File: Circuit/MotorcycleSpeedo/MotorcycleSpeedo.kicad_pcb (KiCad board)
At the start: 2 copper layers, 2 parts

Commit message: Board built enough to submit. I'm sure changes will be made.
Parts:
- removed REF** (x2): x25FrontStepper, X25Stepper:x25FrontStepper
- added BT101: Battery_Cell, Battery:BatteryHolder_Keystone_1060_1x2032, B.Cu at (240.7, 154.4)
- added C101: C, Capacitor_SMD:C_0603_1608Metric, B.Cu at (244.7, 167.8)
- added C102: C, Capacitor_SMD:C_0603_1608Metric, B.Cu at (246.3, 167.8)
- added C103: C, Capacitor_SMD:C_0603_1608Metric, B.Cu at (262.4, 147.8)
- added C104: C, Capacitor_SMD:C_0603_1608Metric, B.Cu at (261.4, 153.6)
- added C105: .1uF, Capacitor_SMD:C_0603_1608Metric, B.Cu at (203.4, 157.6)
- added C106: C, Capacitor_SMD:C_0603_1608Metric, B.Cu at (258.2, 142.6)
- added C107: C, Capacitor_SMD:C_0603_1608Metric, B.Cu at (258.4, 138.5)
- added C108: C, Capacitor_SMD:C_0603_1608Metric, B.Cu at (181.7, 162.2)
- added C109: .1uf, Capacitor_SMD:C_0603_1608Metric, B.Cu at (181.7, 163.8)
- added C110: C, Capacitor_SMD:C_0603_1608Metric, B.Cu at (191.7, 163.4)
- added C111: .1uf, Capacitor_SMD:C_0603_1608Metric, B.Cu at (187.7, 157.0)
- added C112: .1uf, Capacitor_SMD:C_0603_1608Metric, B.Cu at (184.7, 162.7)
- added C113: C, Capacitor_SMD:C_0603_1608Metric, B.Cu at (226.7, 162.2)
- added C114: 100uF, Capacitor_SMD:C_0603_1608Metric, B.Cu at (258.8, 154.2)
- added C115: 1500pf, Capacitor_SMD:C_0603_1608Metric, B.Cu at (259.5, 161.1)
- added C116: CP, Capacitor_SMD:C_0603_1608Metric, B.Cu at (264.4, 166.9)
- added C117: C, Capacitor_SMD:C_0603_1608Metric, B.Cu at (164.7, 173.6)
- added C118: C, Capacitor_SMD:C_0603_1608Metric, B.Cu at (172.8, 173.6)
- added C119: C, Capacitor_SMD:C_0603_1608Metric, B.Cu at (174.3, 169.0)
- added C120: C, Capacitor_SMD:C_0603_1608Metric, B.Cu at (214.8, 162.4)
- added C121: C, Capacitor_SMD:C_0603_1608Metric, B.Cu at (163.3, 156.1)
- added C122: C, Capacitor_SMD:C_0603_1608Metric, B.Cu at (173.1, 152.6)
- added C123: C, Capacitor_SMD:C_0603_1608Metric, B.Cu at (170.0, 142.8)
- added C124: C, Capacitor_SMD:C_0603_1608Metric, B.Cu at (170.0, 141.2)
- added C125: C, Capacitor_SMD:C_0603_1608Metric, B.Cu at (159.2, 143.7)
- added C126: C, Capacitor_SMD:C_0603_1608Metric, B.Cu at (159.2, 145.2)
- added C127: C, Capacitor_SMD:C_0603_1608Metric, B.Cu at (156.9, 144.4)
- added C128: 20pF, Capacitor_SMD:C_0603_1608Metric, B.Cu at (155.4, 151.4)
- added C129: 20pF, Capacitor_SMD:C_0603_1608Metric, B.Cu at (155.4, 148.3)
- added C130: 9pF, Capacitor_SMD:C_0603_1608Metric, B.Cu at (160.6, 157.9)
- added C131: 9pF, Capacitor_SMD:C_0603_1608Metric, B.Cu at (157.5, 158.0)
- added C132: C, Capacitor_SMD:C_0603_1608Metric, B.Cu at (171.6, 124.0)
- added C133: C, Capacitor_SMD:C_0603_1608Metric, B.Cu at (244.2, 125.1)
- added C134: .1uF, Capacitor_SMD:C_0603_1608Metric, B.Cu at (179.9, 117.9)
- added C135: 0.1uF, Capacitor_SMD:C_0603_1608Metric, B.Cu at (180.2, 171.4)
- added C136: 0.22uF, Capacitor_SMD:C_0603_1608Metric, B.Cu at (159.3, 140.7)
- added C137: .1uF, Capacitor_SMD:C_0603_1608Metric, B.Cu at (253.1, 117.7)
- added C138: .1uF, Capacitor_SMD:C_0603_1608Metric, B.Cu at (176.8, 117.9)
- added C139: .1uF, Capacitor_SMD:C_0603_1608Metric, B.Cu at (247.9, 117.6)
- added C140: 0.1uF, Capacitor_SMD:C_0603_1608Metric, B.Cu at (176.6, 171.5)
- added C141: 0.22uF, Capacitor_SMD:C_0603_1608Metric, B.Cu at (160.9, 140.7)
- added C142: .01uF, Capacitor_SMD:C_0603_1608Metric, B.Cu at (202.1, 162.7)
- added C143: .1uF, Capacitor_SMD:C_0603_1608Metric, B.Cu at (213.8, 149.0)
- added C144: .1uF, Capacitor_SMD:C_0603_1608Metric, B.Cu at (213.9, 147.3)
- added C145: C, Capacitor_SMD:C_0603_1608Metric, B.Cu at (157.8, 140.7)
- added C201: 1uF, Capacitor_SMD:C_0603_1608Metric, B.Cu at (261.1, 137.8)
- added C202: 22uF, Capacitor_THT:C_Radial_D5.0mm_H11.0mm_P2.00mm, B.Cu at (257.3, 147.2)
- added C203: DNP, Capacitor_SMD:C_0805_2012Metric, B.Cu at (269.8, 140.5)
- added C204: 22uF, Capacitor_SMD:C_0805_2012Metric, B.Cu at (268.2, 144.8)
- added D101: D_Schottky, Diode_SMD:D_SMA, B.Cu at (241.9, 169.8)
- added D102: D_Schottky, Diode_SMD:D_SMA, B.Cu at (233.2, 169.9)
- added D103: D_TVS, Diode_SMD:D_SMA, B.Cu at (233.2, 166.2)
- added D104: SP721, Package_SO:SOIC-8_3.9x4.9mm_P1.27mm, B.Cu at (158.9, 162.6)
- added D105: LED, LED_SMD:LED_0603_1608Metric_Pad1.05x0.95mm_HandSolder, B.Cu at (270.9, 130.8)
- added D106: LED, LED_SMD:LED_0603_1608Metric_Pad1.05x0.95mm_HandSolder, B.Cu at (273.5, 120.3)
- added D107: LED, LED_SMD:LED_0603_1608Metric_Pad1.05x0.95mm_HandSolder, B.Cu at (273.8, 109.4)
- added D108: LED, LED_SMD:LED_0603_1608Metric_Pad1.05x0.95mm_HandSolder, B.Cu at (271.8, 98.8)
- added D109: LED, LED_SMD:LED_0603_1608Metric_Pad1.05x0.95mm_HandSolder, B.Cu at (267.6, 88.8)
- added D110: LED, LED_SMD:LED_0603_1608Metric_Pad1.05x0.95mm_HandSolder, B.Cu at (261.4, 79.9)
- added D111: LED, LED_SMD:LED_0603_1608Metric_Pad1.05x0.95mm_HandSolder, B.Cu at (253.5, 72.6)
- added D112: LED, LED_SMD:LED_0603_1608Metric_Pad1.05x0.95mm_HandSolder, B.Cu at (244.1, 67.1)
- added D113: LED, LED_SMD:LED_0603_1608Metric_Pad1.05x0.95mm_HandSolder, B.Cu at (233.9, 63.7)
- added D114: LED, LED_SMD:LED_0603_1608Metric_Pad1.05x0.95mm_HandSolder, B.Cu at (223.1, 62.5)
- added D115: LED, LED_SMD:LED_0603_1608Metric_Pad1.05x0.95mm_HandSolder, F.Cu at (225.6, 115.1)
- added D116: LED, LED_SMD:LED_0603_1608Metric_Pad1.05x0.95mm_HandSolder, F.Cu at (225.6, 111.6)
- added D117: LED, LED_SMD:LED_0603_1608Metric_Pad1.05x0.95mm_HandSolder, B.Cu at (156.1, 130.8)
- added D118: LED, LED_SMD:LED_0603_1608Metric_Pad1.05x0.95mm_HandSolder, B.Cu at (153.5, 120.3)
- added D119: D, Diode_SMD:D_SMA, B.Cu at (227.8, 166.7)
- added D120: LED, LED_SMD:LED_0603_1608Metric_Pad1.05x0.95mm_HandSolder, B.Cu at (153.2, 109.4)
- added D121: LED, LED_SMD:LED_0603_1608Metric_Pad1.05x0.95mm_HandSolder, B.Cu at (155.2, 98.8)
- added D122: D, Diode_SMD:D_SMA, B.Cu at (270.1, 162.4)
- added D123: LED, LED_SMD:LED_0603_1608Metric_Pad1.05x0.95mm_HandSolder, B.Cu at (159.4, 88.8)
- added D124: LED, LED_SMD:LED_0603_1608Metric_Pad1.05x0.95mm_HandSolder, B.Cu at (165.6, 80.0)
- added D125: LED, LED_SMD:LED_0603_1608Metric_Pad1.05x0.95mm_HandSolder, B.Cu at (173.5, 72.6)
- added D126: LED, LED_SMD:LED_0603_1608Metric_Pad1.05x0.95mm_HandSolder, B.Cu at (182.8, 67.1)
- added D127: LED, LED_SMD:LED_0603_1608Metric_Pad1.05x0.95mm_HandSolder, B.Cu at (193.1, 63.7)
- added D128: LED, LED_SMD:LED_0603_1608Metric_Pad1.05x0.95mm_HandSolder, B.Cu at (203.8, 62.6)
- added D129: LED, LED_SMD:LED_0603_1608Metric_Pad1.05x0.95mm_HandSolder, F.Cu at (201.9, 115.0)
- added D130: LED, LED_SMD:LED_0603_1608Metric_Pad1.05x0.95mm_HandSolder, F.Cu at (202.4, 111.3)
- added D131: D, Diode_SMD:D_SMA, B.Cu at (216.4, 166.9)
- added D132: HIGH, Indicators:HF.SilkSF.Cu, F.Cu at (206.9, 82.0)
- added D133: RIGHT, Indicators:RightPointingF.SilkSF.Cu, F.Cu at (232.4, 82.0)
- added D134: LEFT, Indicators:LeftPointingF.SilkSF.Cu, F.Cu at (194.4, 82.5)
- added D135: NEUTRAL, Indicators:NF.SilkSF.Cu, F.Cu at (220.4, 82.0)
- added F101: Polyfuse, Fuse:Fuse_1206_3216Metric, B.Cu at (238.1, 169.9)
- added H101: MountingHole_Pad, MountingHole:MountingHole_3.2mm_M3_DIN965_Pad, F.Cu at (243.8, 96.4)
- added H102: MountingHole_Pad, MountingHole:MountingHole_3.2mm_M3_DIN965_Pad, F.Cu at (213.8, 125.0)
- added H103: MountingHole_Pad, MountingHole:MountingHole_3.2mm_M3_DIN965_Pad, F.Cu at (213.8, 60.4)
- added H104: MountingHole_Pad, MountingHole:MountingHole_3.2mm_M3_DIN965_Pad, F.Cu at (273.9, 171.6)
- added H105: MountingHole_Pad, MountingHole:MountingHole_3.2mm_M3_DIN965_Pad, F.Cu at (180.9, 96.5)
- added H106: MountingHole_Pad, MountingHole:MountingHole_3.2mm_M3_DIN965_Pad, F.Cu at (157.2, 171.2)
- added J101: Conn_01x07_Female, Connector_PinHeader_2.54mm:PinHeader_1x07_P2.54mm_Vertical, F.Cu at (187.5, 167.4)
- added J102: Conn_01x03_Female, Connector_PinHeader_2.54mm:PinHeader_1x03_P2.54mm_Vertical, B.Cu at (227.1, 172.4)
- added J103: Conn_01x02_Female, Connector_PinHeader_2.54mm:PinHeader_1x02_P2.54mm_Vertical, B.Cu at (167.5, 174.7)
- added J104: Conn_01x03_Female, Connector_PinHeader_2.54mm:PinHeader_1x03_P2.54mm_Vertical, B.Cu at (215.2, 172.5)
- added J105: Conn_01x04_Female, Connector_PinHeader_2.54mm:PinHeader_1x04_P2.54mm_Vertical, B.Cu at (218.1, 73.0)
- added J106: Conn_02x04_Counter_Clockwise, Connector_PinHeader_2.54mm:PinHeader_2x04_P2.54mm_Vertical, B.Cu at (185.3, 148.4)
- added J107: Conn_01x03_Female, Connector_PinHeader_2.54mm:PinHeader_1x03_P2.54mm_Vertical, F.Cu at (238.0, 173.7)
- added J108: Conn_01x04_Male, Connector_PinHeader_1.27mm:PinHeader_1x04_P1.27mm_Vertical, F.Cu at (174.1, 159.7)
- added J109: Conn_01x04_Female, Connector_PinHeader_2.54mm:PinHeader_1x04_P2.54mm_Vertical, F.Cu at (175.8, 174.1)
- added J110: Conn_01x01_Female, TestPoint:TestPoint_Pad_1.5x1.5mm, B.Cu at (163.8, 160.3)
- added JP101: SolderJumper_3_Bridged12, Jumper:SolderJumper-3_P1.3mm_Bridged12_Pad1.0x1.5mm_NumberLabels, B.Cu at (177.8, 162.9)
- added JP102: SolderJumper_3_Bridged12, Jumper:SolderJumper-3_P1.3mm_Bridged12_Pad1.0x1.5mm_NumberLabels, B.Cu at (187.9, 164.6)
- added JP103: SolderJumper_3_Bridged12, Jumper:SolderJumper-3_P1.3mm_Bridged12_Pad1.0x1.5mm_NumberLabels, B.Cu at (207.6, 172.3)
- added JP104: SolderJumper_3_Bridged12, Jumper:SolderJumper-3_P1.3mm_Bridged12_RoundedPad1.0x1.5mm_NumberLabels, B.Cu at (203.4, 91.0)
- added JP105: SolderJumper_3_Bridged12, Jumper:SolderJumper-3_P1.3mm_Bridged12_RoundedPad1.0x1.5mm_NumberLabels, B.Cu at (229.4, 90.5)
- added JP106: SolderJumper_3_Bridged12, Jumper:SolderJumper-3_P1.3mm_Bridged12_RoundedPad1.0x1.5mm_NumberLabels, B.Cu at (198.4, 91.0)
- added JP107: SolderJumper_3_Bridged12, Jumper:SolderJumper-3_P1.3mm_Bridged12_RoundedPad1.0x1.5mm_NumberLabels, B.Cu at (224.4, 90.5)
- added L101: 220, MotorcycleSpeedo:SMSD0804-Inductor, B.Cu at (271.7, 153.3)
- added L201: 10uH, CDRH6D28:CDRH6D28, B.Cu at (263.1, 140.4)
- added M101: Stepper_Motor_bipolar, X25Stepper:x25FrontStepper, F.Cu at (203.8, 113.4)
- added M102: Stepper_Motor_bipolar, X25Stepper:x25FrontStepper, B.Cu at (223.8, 113.4)
- added Q101: Q_NMOS_GSD, Package_TO_SOT_SMD:SOT-23, B.Cu at (252.7, 109.4)
- added Q102: Q_NMOS_GSD, Package_TO_SOT_SMD:SOT-23, B.Cu at (164.1, 119.0)
- added Q103: Q_PMOS_GSD, Package_TO_SOT_SMD:SOT-23, B.Cu at (193.1, 90.3)
- added Q104: Q_NMOS_GSD, Package_TO_SOT_SMD:SOT-23, B.Cu at (193.1, 94.3)
- added R101: R, Resistor_SMD:R_0603_1608Metric, B.Cu at (238.4, 166.8)
- added R102: R, Resistor_SMD:R_0603_1608Metric, B.Cu at (261.6, 125.2)
- added R103: R, Resistor_SMD:R_0603_1608Metric, B.Cu at (261.8, 109.1)
- added R104: R, Resistor_SMD:R_0603_1608Metric, B.Cu at (254.0, 91.8)
- added R105: R, Resistor_SMD:R_0603_1608Metric, B.Cu at (240.2, 80.2)
- added R106: R, Resistor_SMD:R_0603_1608Metric, B.Cu at (240.2, 78.5)
- added R107: 10K, Resistor_SMD:R_0603_1608Metric, B.Cu at (244.9, 137.7)
- added R108: R, Resistor_SMD:R_0603_1608Metric, B.Cu at (219.4, 127.5)
- added R109: 470, Resistor_SMD:R_0603_1608Metric, B.Cu at (244.9, 139.3)
- added R110: 10K, Resistor_SMD:R_0603_1608Metric, B.Cu at (252.5, 112.0)
- added R111: .22, Resistor_SMD:R_0603_1608Metric, B.Cu at (264.5, 153.6)
- added R112: 10K, Resistor_SMD:R_0603_1608Metric, B.Cu at (226.7, 160.6)
- added R113: R, Resistor_SMD:R_0603_1608Metric, B.Cu at (224.9, 168.7)
- added R114: R, Resistor_SMD:R_0603_1608Metric, B.Cu at (165.9, 128.0)
- added R115: 180, Resistor_SMD:R_0603_1608Metric, B.Cu at (265.1, 151.9)
- added R116: R, Resistor_SMD:R_0603_1608Metric, B.Cu at (163.1, 109.4)
- added R117: R, Resistor_SMD:R_0603_1608Metric, B.Cu at (168.0, 93.3)
- added R118: R, Resistor_SMD:R_0603_1608Metric, B.Cu at (262.0, 166.2)
- added R119: R, Resistor_SMD:R_0603_1608Metric, B.Cu at (178.6, 80.1)
- added R120: 120, Resistor_SMD:R_0603_1608Metric, B.Cu at (164.4, 168.9)
- added R121: R, Resistor_SMD:R_0603_1608Metric, B.Cu at (262.0, 167.8)
- added R122: R, Resistor_SMD:R_0603_1608Metric, B.Cu at (195.6, 71.5)
- added R123: R, Resistor_SMD:R_0603_1608Metric, B.Cu at (207.4, 127.5)
- added R124: 10K, Resistor_SMD:R_0603_1608Metric, B.Cu at (163.9, 121.5)
- added R125: 10K, Resistor_SMD:R_0603_1608Metric, B.Cu at (214.8, 160.8)
- added R126: R, Resistor_SMD:R_0603_1608Metric, B.Cu at (213.7, 168.8)
- added R127: R, Resistor_SMD:R_0603_1608Metric, B.Cu at (216.3, 148.1)
- added R128: R, Resistor_SMD:R_0603_1608Metric, B.Cu at (220.3, 150.7)
- added R129: 1k, Resistor_SMD:R_0603_1608Metric, B.Cu at (189.4, 91.0)
- added R130: R, Resistor_SMD:R_0603_1608Metric, B.Cu at (155.3, 144.4)
- added R131: 10K, Resistor_SMD:R_0603_1608Metric, B.Cu at (189.4, 89.3)
- added R132: R, Resistor_SMD:R_0603_1608Metric, B.Cu at (203.4, 88.0)
- added R133: 10K, Resistor_SMD:R_0603_1608Metric, B.Cu at (187.0, 140.5)
- added R134: 10K, Resistor_SMD:R_0603_1608Metric, B.Cu at (187.0, 138.5)
- added R135: 10K, Resistor_SMD:R_0603_1608Metric, B.Cu at (187.0, 136.5)
- added R136: 10K, Resistor_SMD:R_0603_1608Metric, B.Cu at (187.0, 142.5)
- added R137: R, Resistor_SMD:R_0603_1608Metric, B.Cu at (229.4, 87.5)
- added R138: R, Resistor_SMD:R_0603_1608Metric, B.Cu at (198.4, 88.0)
- added R139: R, Resistor_SMD:R_0603_1608Metric, B.Cu at (224.4, 87.5)
- added R140: 10K, Resistor_SMD:R_0603_1608Metric, B.Cu at (189.4, 93.5)
- added R141: 1k, Resistor_SMD:R_0603_1608Metric, B.Cu at (189.4, 95.3)
- added R142: 2.49K, Resistor_SMD:R_0603_1608Metric, B.Cu at (180.2, 169.9)
- added R143: 470, Resistor_SMD:R_0603_1608Metric, B.Cu at (180.2, 168.3)
- added R144: 2.49K, Resistor_SMD:R_0603_1608Metric, B.Cu at (176.7, 169.9)
- added R145: 470, Resistor_SMD:R_0603_1608Metric, B.Cu at (176.7, 168.3)
- added R146: 560, Resistor_SMD:R_0603_1608Metric, B.Cu at (193.4, 163.5)
- added R147: 560, Resistor_SMD:R_0603_1608Metric, B.Cu at (195.0, 163.5)
- added R148: 560, Resistor_SMD:R_0603_1608Metric, B.Cu at (196.6, 163.5)
- added R149: 560, Resistor_SMD:R_0603_1608Metric, B.Cu at (198.2, 163.5)
- added R150: 560, Resistor_SMD:R_0603_1608Metric, B.Cu at (199.7, 163.5)
- added R151: 22, Resistor_SMD:R_0603_1608Metric, B.Cu at (177.0, 156.8)
- added R152: 22, Resistor_SMD:R_0603_1608Metric, B.Cu at (175.5, 156.8)
- added R201: 40.2K, Resistor_SMD:R_0603_1608Metric, B.Cu at (267.9, 140.5)
- added R202: 59K, Resistor_SMD:R_0603_1608Metric, B.Cu at (265.3, 137.8)
- added R203: 13K, Resistor_SMD:R_0603_1608Metric, B.Cu at (268.6, 137.9)
- added U101: AP131-33, Package_TO_SOT_SMD:SOT-23-5, B.Cu at (261.5, 150.7)
- added U103: APT8L08, Package_SO:SOIC-14_3.9x8.7mm_P1.27mm, B.Cu at (197.6, 157.9)
- added U104: BMP280, Package_LGA:Bosch_LGA-8_2x2.5mm_P0.65mm_ClockwisePinNumbering, B.Cu at (181.8, 159.3)
- added U105: MPU-9250, Sensor_Motion:InvenSense_QFN-24_3x3mm_P0.4mm, B.Cu at (188.0, 160.0)
- added U106: LTV-817, Package_DIP:DIP-4_W7.62mm, B.Cu at (222.6, 169.3)
- added U107: MC34063AD, Package_SO:SOIC-8_3.9x4.9mm_P1.27mm, B.Cu at (263.1, 158.5)
- added U108: TJA1051T-E, Package_SO:SOIC-8_3.9x4.9mm_P1.27mm, B.Cu at (169.4, 169.0)
- added U109: LTV-817, Package_DIP:DIP-4_W7.62mm, B.Cu at (211.3, 169.0)
- added U110: FM116B, Package_TO_SOT_SMD:SOT-23-6, B.Cu at (213.7, 152.7)
- added U111: 74AHCT1G14, Package_TO_SOT_SMD:SOT-353_SC-70-5, B.Cu at (213.6, 156.1)
- added U112: STM32F103C8Tx, Package_QFP:LQFP-48_7x7mm_P0.5mm, B.Cu at (166.5, 149.2)
- added U113: TC1508S, Package_SO:SOP-16_4.55x10.3mm_P1.27mm, B.Cu at (178.2, 123.8)
- added U114: TC1509S, Package_SO:SOP-16_4.55x10.3mm_P1.27mm, B.Cu at (250.7, 123.0)
- added U1[2: AMS1117-5.0, Package_TO_SOT_SMD:SOT-223, B.Cu at (252.7, 140.8)
- added U201: AP65111AWU, Package_TO_SOT_SMD:TSOT-23-6_HandSoldering, B.Cu at (259.9, 135.2)
- added V101: HV5812, Package_SO:SOIC-28W_7.5x17.9mm_P1.27mm, B.Cu at (224.0, 140.0)
- added V102: HNA-12MM54T, HNA-12MM54T_VFD:HNA-12MM54T, F.Cu at (214.0, 131.0)
- added V103: HV5812, Package_SO:SOIC-28W_7.5x17.9mm_P1.27mm, B.Cu at (203.0, 140.0)
- added Y101: 8M, Crystal:Crystal_SMD_5032-2Pin_5.0x3.2mm, B.Cu at (158.2, 149.8)
- added Y102: 32K, Crystal:Crystal_SMD_5032-2Pin_5.0x3.2mm, B.Cu at (159.1, 155.1)
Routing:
- net GND: track 0.00 -> 844.2 mm, vias 0 -> 238
- net +5V: track 0.00 -> 525.9 mm, vias 0 -> 23
- net +3V3: track 0.00 -> 292.3 mm, vias 0 -> 18
- net +12V: track 0.00 -> 229.0 mm, vias 0 -> 4
- net Net-(D106-Pad1): track 0.00 -> 154.7 mm, vias 0 -> 5
- net /12V_Sense: track 0.00 -> 146.3 mm, vias 0 -> 4
- net Net-(D118-Pad1): track 0.00 -> 145.2 mm, vias 0 -> 3
- net /LED2: track 0.00 -> 126.3 mm, vias 0 -> 3
- net /JTDI: track 0.00 -> 122.2 mm, vias 0 -> 4
- net /JTCK: track 0.00 -> 118.8 mm, vias 0 -> 2
- net /JTMS: track 0.00 -> 117.8 mm, vias 0 -> 3
- net /STP-IN5: track 0.00 -> 113.4 mm, vias 0 -> 4
- net /HV_GRID: track 0.00 -> 95.2 mm, vias 0 -> 4
- net /VFD_LV_BLANK: track 0.00 -> 92.6 mm, vias 0 -> 5
- net /VFD_LV_STROBE: track 0.00 -> 89.5 mm, vias 0 -> 4
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- added copper zone on B.Cu, net GND
- added copper zone on F.Cu, net GND
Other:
- board outline added: 136.8 x 121.3 mm
- net class Default: clearance 0.2 -> 0.16; trace_width 0.25 -> 0.16
- rule trace_clearance: 0.2 -> 0.16
- rule trace_min: 0.2 -> 0.16
- board text added: "12V GND COM"
- board text added: "12V RPM GND"
- board text added: "2019 AB1TJ Motorcycle Speedometer Rev.0 Be too lazy to fail."
- board text added: "5V COM 12V"
- board text added: "CAN- CAN+"
- board text added: "GND D+ D- 5V"
- board text added: "GND TMP2+ GND TMP1+"
- board text added: "H N R L"
- board text added: "SW12V 12V GND"
- board text added: "V+ VSS GND"

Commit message: Modified the board.
I noticed I had the TDI and TMS? lines PA14 and PA15 switched. I
modified the schematic and board. They should both match what was
actually created.
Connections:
- J106 pad 4: /JTCK -> /JTDI
- J106 pad 6: /JTDI -> /JTCK
- U112 pad 37: /JTDI -> /JTCK
- U112 pad 38: /JTCK -> /JTDI
- U114 pad 6: /JTDI -> /JTCK
- U114 pad 7: /JTCK -> /JTDI
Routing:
- net /JTDI: track 122.2 -> 118.8 mm, vias 4 -> 2
- net /JTCK: track 118.8 -> 122.2 mm, vias 2 -> 4

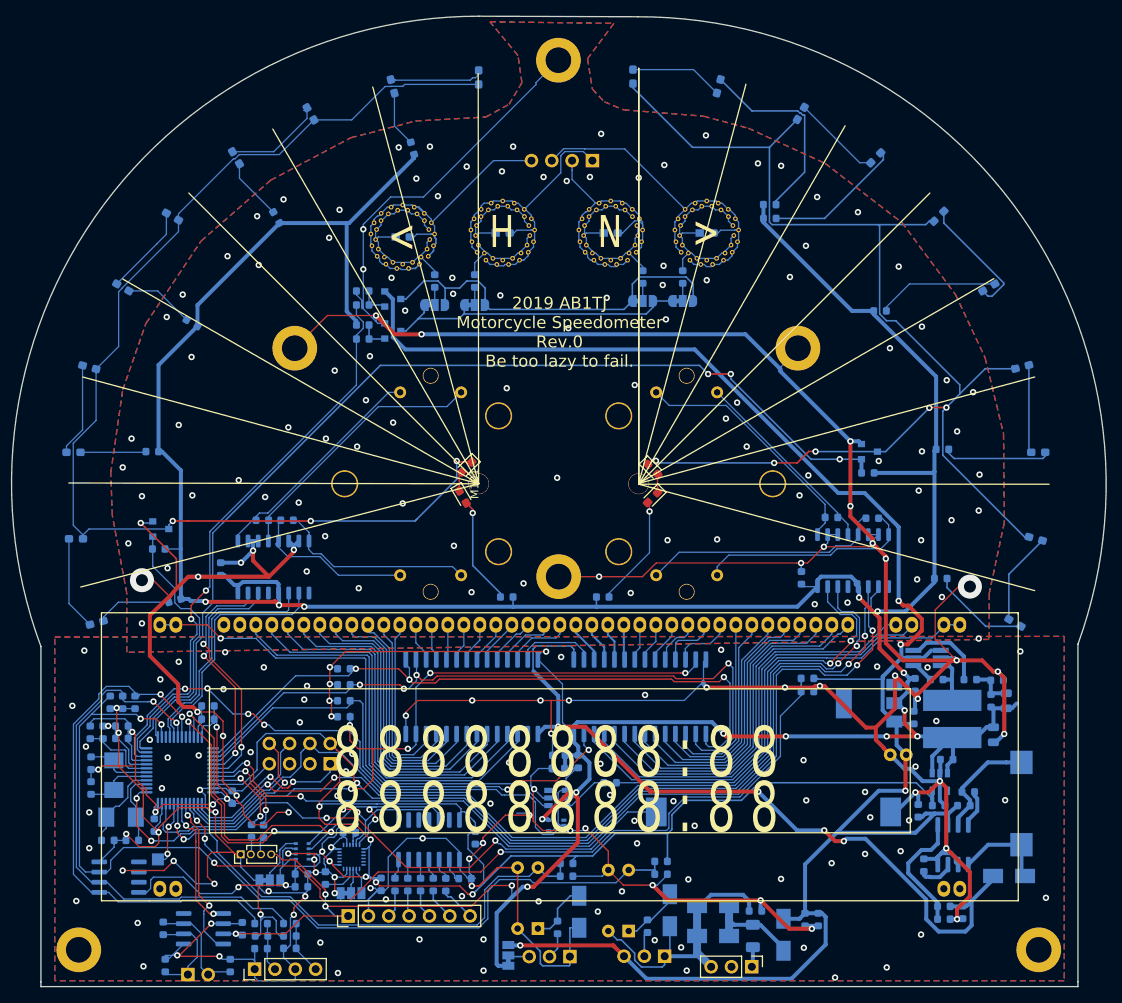
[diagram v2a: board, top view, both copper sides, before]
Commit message: Finished rev 1 of the board, changed motor drivers, moved power supply stouff, fixed programming header layout, added power indication LEDS
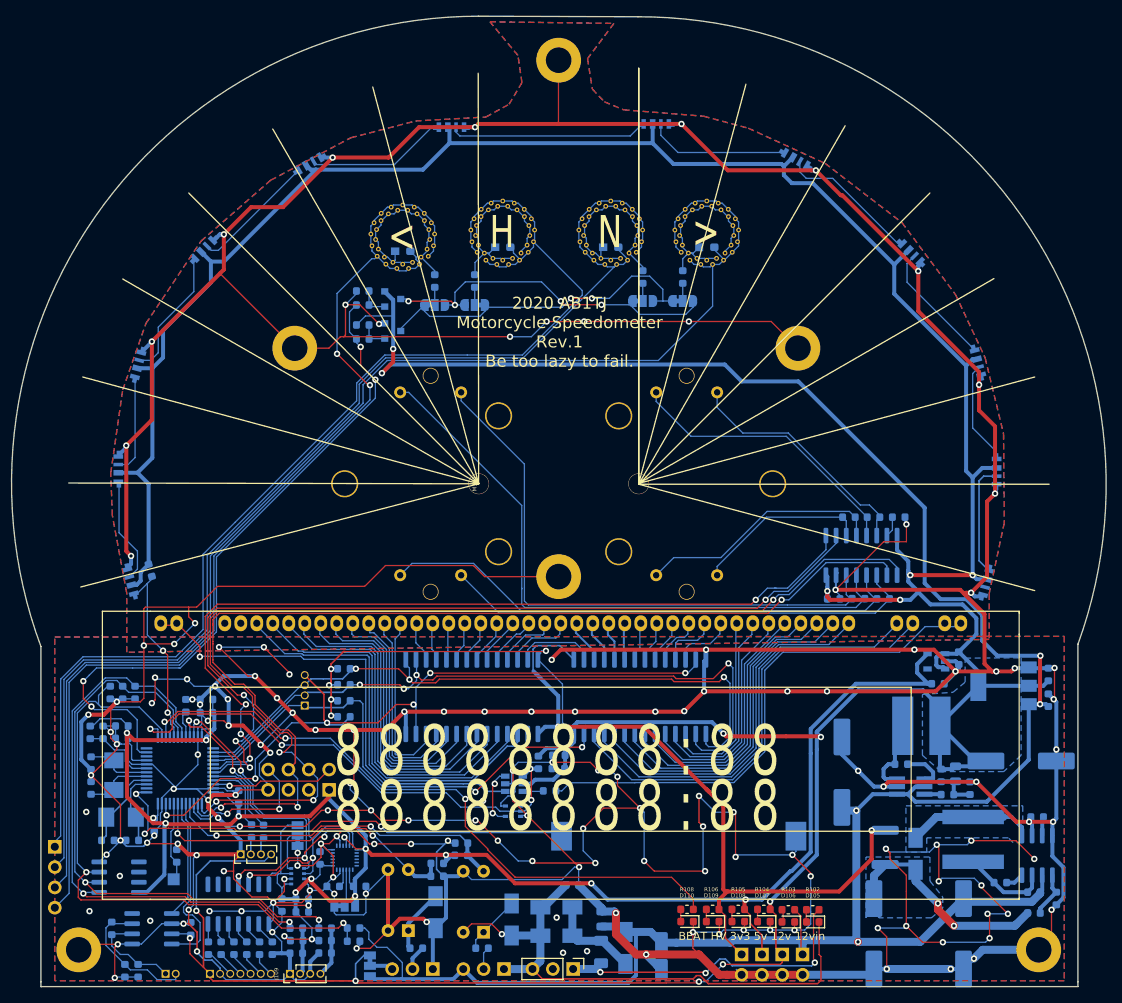
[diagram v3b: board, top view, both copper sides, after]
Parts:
- removed C133: C, Capacitor_SMD:C_0603_1608Metric
- removed D111, D112, D113, D114, D115, D116, D117, D118, D120, D121, D123, D124, D125, D126, D127, D128, D129, D130: LED, LED_SMD:LED_0603_1608Metric_Pad1.05x0.95mm_HandSolder
- removed Q101, Q102: Q_NMOS_GSD, Package_TO_SOT_SMD:SOT-23
- removed R119, R122, R123: R, Resistor_SMD:R_0603_1608Metric
- removed R124: 10K, Resistor_SMD:R_0603_1608Metric
- added F102: Polyfuse, Fuse:Fuse_1812_4532Metric, B.Cu at (254.7, 158.8)
- added J111: Conn_01x02_Male, Connector_PinSocket_2.54mm:PinSocket_1x02_P2.54mm_Vertical, B.Cu at (239.3, 172.2)
- added J112: Conn_01x02_Male, Connector_PinSocket_2.54mm:PinSocket_1x02_P2.54mm_Vertical, B.Cu at (244.3, 172.2)
- added J113: Conn_01x02_Male, Connector_PinSocket_2.54mm:PinSocket_1x02_P2.54mm_Vertical, B.Cu at (241.8, 172.2)
- added J114: Conn_01x02_Male, Connector_PinSocket_2.54mm:PinSocket_1x02_P2.54mm_Vertical, B.Cu at (236.7, 172.2)
- added J115: Conn_01x04_Female, Connector_PinSocket_1.27mm:PinSocket_1x04_P1.27mm_Vertical, B.Cu at (182.1, 141.1)
- added U102: SK6812-A, SK6812-SideA:SK6812-SideA, B.Cu at (161.4, 127.2)
- added U115: SK6812-A, SK6812-SideA:SK6812-SideA, B.Cu at (168.6, 85.8)
- added U117: SK6812-A, SK6812-SideA:SK6812-SideA, B.Cu at (181.4, 74.8)
- added U118: SK6812-A, SK6812-SideA:SK6812-SideA, B.Cu at (198.6, 69.4)
- added U119: SK6812-A, SK6812-SideA:SK6812-SideA, B.Cu at (224.2, 69.0)
- added U120: SK6812-A, SK6812-SideA:SK6812-SideA, B.Cu at (241.6, 72.4)
- added U121: SK6812-A, SK6812-SideA:SK6812-SideA, B.Cu at (256.2, 83.6)
- added U122: SK6812-A, SK6812-SideA:SK6812-SideA, B.Cu at (265.2, 96.6)
- added U123: SK6812-A, SK6812-SideA:SK6812-SideA, B.Cu at (268.0, 110.0)
- added U124: SK6812-A, SK6812-SideA:SK6812-SideA, B.Cu at (267.2, 123.8)
- added U125: VID6608, Package_SO:SOIC-16_3.9x9.9mm_P1.27mm, B.Cu at (251.7, 122.3)
- C101: footprint Capacitor_SMD:C_0603_1608Metric -> Capacitor_SMD:C_0805_2012Metric
- C102: value C -> 33uH; footprint Capacitor_SMD:C_0603_1608Metric -> Capacitor_SMD:C_Elec_4x5.4
- C114: value 100uF -> CP1; footprint Capacitor_SMD:C_0603_1608Metric -> Capacitor_SMD:C_Elec_10x10.2
- C115: value 1500pf -> 680pf
- C116: value CP -> 330uF; footprint Capacitor_SMD:C_0603_1608Metric -> Capacitor_SMD:C_Elec_10x10.2
- C123, C126, C127: value C -> 0.1uF
- C124, C125: value C -> 1uF
- C202: footprint Capacitor_THT:C_Radial_D5.0mm_H11.0mm_P2.00mm -> Capacitor_SMD:C_Elec_10x10.2
- C204: footprint Capacitor_SMD:C_0805_2012Metric -> Capacitor_SMD:C_Elec_10x10.2
- D105, D106, D107, D108, D109, D110: footprint LED_SMD:LED_0603_1608Metric_Pad1.05x0.95mm_HandSolder -> LED_SMD:LED_0603_1608Metric; moved to F.Cu
- J101: footprint Connector_PinHeader_2.54mm:PinHeader_1x07_P2.54mm_Vertical -> Connector_PinSocket_1.27mm:PinSocket_1x07_P1.27mm_Vertical; moved to B.Cu
- J103: footprint Connector_PinHeader_2.54mm:PinHeader_1x02_P2.54mm_Vertical -> Connector_PinHeader_1.27mm:PinHeader_1x02_P1.27mm_Vertical
- J109: footprint Connector_PinHeader_2.54mm:PinHeader_1x04_P2.54mm_Vertical -> Connector_PinHeader_1.27mm:PinHeader_1x04_P1.27mm_Vertical
- L101: value 220 -> 330uh; footprint MotorcycleSpeedo:SMSD0804-Inductor -> Inductor_SMD:L_Taiyo-Yuden_NR-80xx
- R102, R103, R104, R105, R106, R108: value R -> 1K; moved to F.Cu
- R110: value 10K -> R
- R114, R116: value R -> 10K
- R118: value R -> 59K
- R121: value R -> 2.49K
- U113: value TC1508S -> SK6812-A; footprint Package_SO:SOP-16_4.55x10.3mm_P1.27mm -> SK6812-SideA:SK6812-SideA
- U114: value TC1509S -> SK6812-A; footprint Package_SO:SOP-16_4.55x10.3mm_P1.27mm -> SK6812-SideA:SK6812-SideA
- moved J105 109.0 mm to (150.9, 158.8), turned to 180 degrees
- moved D110 93.6 mm to (229.9, 168.1), turned to 180 degrees
- moved U114 92.1 mm to (161.4, 100.4), turned to 75 degrees
- moved R117 91.6 mm to (256.4, 117.6), turned to 0 degrees
- moved R110 90.5 mm to (162.8, 124.2), turned to -75 degrees
- moved R106 88.4 mm to (233.1, 166.6)
- moved R105 86.5 mm to (236.3, 166.6)
- moved D109 86.5 mm to (233.1, 168.1), turned to 180 degrees
- moved D108 77.9 mm to (236.3, 168.1), turned to 180 degrees
- moved C132 76.7 mm to (248.2, 127.8), turned to 0 degrees
- moved R104 76.2 mm to (239.5, 166.6)
- moved C134 75.2 mm to (254.4, 127.8)
- moved C138 75.2 mm to (251.3, 127.7), turned to 180 degrees
- moved D107 67.9 mm to (239.5, 168.1), turned to 180 degrees
- moved R107 64.8 mm to (188.2, 168.9)
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- renumbered U1[2 to U116
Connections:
- C116 pad 1: /HV_GRID -> Net-(C116-Pad1)
- D104 pad 5: (no net) -> /TVS4
- D104 pad 6: (no net) -> /TVS5
- D104 pad 7: (no net) -> /TVS6
- D105 pad 1: Net-(D105-Pad1) -> GNDPWR
- D106 pad 1: Net-(D106-Pad1) -> GND
- D106 pad 2: Net-(D105-Pad1) -> Net-(D106-Pad2)
- D107 pad 1: Net-(D107-Pad1) -> GND
- D108 pad 1: Net-(D106-Pad1) -> GND
- D108 pad 2: Net-(D107-Pad1) -> Net-(D108-Pad2)
- D109 pad 1: Net-(D109-Pad1) -> GND
- D110 pad 1: Net-(D106-Pad1) -> GND
- D110 pad 2: Net-(D109-Pad1) -> Net-(D110-Pad2)
- D122 pad 1: /HV_GRID -> Net-(C116-Pad1)
- J106 pad 3: (no net) -> Net-(J106-Pad3)
- J106 pad 4: /JTDI -> /JTCK
- J106 pad 5: (no net) -> Net-(J106-Pad5)
- J106 pad 6: /JTCK -> /JTDI
- J107 pad 2: (no net) -> /CONST_12V
- R102 pad 1: Net-(D105-Pad2) -> /SWITCHED_12V
- R102 pad 2: +5V -> Net-(D105-Pad2)
- R103 pad 1: Net-(D107-Pad2) -> +12V
- R103 pad 2: +5V -> Net-(D106-Pad2)
- R104 pad 1: Net-(D109-Pad2) -> +5V
- R104 pad 2: +5V -> Net-(D107-Pad2)
- R105 pad 1: Net-(D111-Pad2) -> +3V3
- R105 pad 2: +5V -> Net-(D108-Pad2)
- R106 pad 1: Net-(D113-Pad2) -> /HV_GRID
- R106 pad 2: +5V -> Net-(D109-Pad2)
- R108 pad 1: Net-(D115-Pad2) -> /HEARTBEAT
- R108 pad 2: +5V -> Net-(D110-Pad2)
- R110 pad 1: /LED2 -> +5V
- R110 pad 2: +5V -> /RGB_LED_DATA
- R114 pad 1: Net-(D117-Pad2) -> /BOOT0
- R114 pad 2: +5V -> GND
- R116 pad 1: Net-(D120-Pad2) -> /BOOT1
- R116 pad 2: +5V -> GND
- R117 pad 1: Net-(D123-Pad2) -> /STP_RST
- R117 pad 2: +5V -> GND
- R118 pad 1: /HV_GRID -> Net-(C116-Pad1)
- R140 pad 2: +5V -> +12V
- U101 pad 4: (no net) -> Net-(U101-Pad4)
- U103 pad 10: (no net) -> Net-(U103-Pad10)
- U103 pad 13: (no net) -> Net-(U103-Pad13)
- U103 pad 8: (no net) -> Net-(U103-Pad8)
- U103 pad 9: (no net) -> Net-(U103-Pad9)
- U105 pad 12: (no net) -> Net-(U105-Pad12)
- U105 pad 21: (no net) -> Net-(U105-Pad21)
- U105 pad 7: (no net) -> Net-(U105-Pad7)
- U108 pad 8: (no net) -> Net-(U108-Pad8)
- U112 pad 10: /VFD_FILAMENT_A -> /LED2
- U112 pad 13: /LED2 -> /VFD_FILAMENT_A
- U112 pad 15: (no net) -> /HEARTBEAT
- U112 pad 16: /STP-IN2 -> Net-(U112-Pad16)
- U112 pad 17: /STP-IN1 -> /RGB_LED_DATA
- U112 pad 2: (no net) -> Net-(U112-Pad2)
- U112 pad 20: (no net) -> /BOOT1
- U112 pad 25: (no net) -> Net-(U112-Pad25)
- U112 pad 29: /STP-IN3 -> Net-(U112-Pad29)
- U112 pad 30: /STP-IN4 -> /L_DIR
- U112 pad 31: /STP-IN5 -> /L_STP
- U112 pad 45: (no net) -> Net-(U112-Pad45)
- U113 pad 1: (no net) -> Net-(U102-Pad3)
- U113 pad 2: /STP-IN1 -> +5V
- U113 pad 3: /STP-IN2 -> Net-(U113-Pad3)
- U113 pad 4: +5V -> GND
- U114 pad 1: (no net) -> Net-(U113-Pad3)
- U114 pad 2: /STP-IN5 -> +5V
- U114 pad 3: /JTMS -> Net-(U114-Pad3)
- U114 pad 4: +5V -> GND
- U116 pad 4: (no net) -> +5V
- V102 pad 46: (no net) -> Net-(V102-Pad46)
- V102 pad 47: (no net) -> Net-(V102-Pad47)
- V103 pad 2: (no net) -> Net-(V103-Pad2)
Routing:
- net GND: track 844.2 -> 1441.2 mm, vias 238 -> 163
- net Net-(D106-Pad1): track 154.7 -> 0.00 mm, vias 5 -> 0
- net Net-(D118-Pad1): track 145.2 -> 0.00 mm, vias 3 -> 0
- net /LED2: track 126.3 -> 0.00 mm, vias 3 -> 0
- net /R_TURN: track 48.9 -> 165.5 mm
- net /STP-IN5: track 113.4 -> 0.00 mm, vias 4 -> 0
- net /L_STP: track 0.00 -> 112.2 mm, vias 0 -> 4
- net /NEUTRAL: track 37.1 -> 148.3 mm
- net /L_DIR: track 0.00 -> 109.1 mm, vias 0 -> 4
- net /HIGH: track 42.1 -> 149.5 mm
- net /JTMS: track 117.8 -> 15.4 mm, vias 3 -> 1
- net /L_TURN: track 46.0 -> 135.9 mm, vias 0 -> 2
- net /HEARTBEAT: track 0.00 -> 81.7 mm, vias 0 -> 3
- net +12V: track 229.0 -> 304.7 mm, vias 4 -> 6
- net /12V_Sense: track 146.3 -> 79.6 mm, vias 4 -> 2
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- added copper zone on B.Cu, net +5V
- added copper zone on B.Cu, net Net-(C116-Pad1)
- added copper zone on B.Cu, net Net-(D122-Pad2)
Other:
- net class Default removed
- board text added: "2020 AB1TJ Motorcycle Speedometer Rev.1 Be too lazy to fail."
- board text added: "3v3 ADDR GND"
- board text added: "5V VOL 12V"
- board text added: "ACTLOW SEL ACTHIGH LTURN"
- board text added: "ACTLOW SEL ACTHIGH NEUTRAL"
- board text added: "ACTLOW SEL ACTHIGH R_TURN"
- board text added: "BEAT HV 3v3 5v 12v 12vin"
- board text added: "GND RPM 12V"
- board text added: "GND VSS VOL"
- board text added: "GND X 4"
- board text added: "HIGH NTRL RTRN LTRN"
- board text added: "LV_BLANK LV_CLK LV_STROBE LV_MOSI"
- board text added: "SW12 C12 PWRGND"
- board text added: "SW12V 5V 3V3 HV_GRID"
- board text added: "TMP1 GND TMP2 GND"
- board text added: "TMS TCK TDI TDO 3v3 NC NC GND"
- board text removed: "12V GND COM"
- board text removed: "12V RPM GND"
- board text removed: "2019 AB1TJ Motorcycle Speedometer Rev.0 Be too lazy to fail."
- board text removed: "5V COM 12V"
- board text removed: "GND TMP2+ GND TMP1+"
- board text removed: "SW12V 12V GND"
- board text removed: "V+ VSS GND"
